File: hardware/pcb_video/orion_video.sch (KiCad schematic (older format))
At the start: 125 parts

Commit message: Оптимизирована логика видеовыхода
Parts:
- removed DD? (x3): LI1, Housings_SOIC:SOIC-14_3.9x8.7mm_Pitch1.27mm, symbol LI1
- added U?: 74AHC1G02, symbol 74AHC1G02
- added U?: 74AHC1G08, symbol 74AHC1G08
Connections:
- wire segments 937 -> 1030

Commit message: Завершена черновая схема видеомодуля.
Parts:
- removed DD? (x3): LI1, Housings_SOIC:SOIC-14_3.9x8.7mm_Pitch1.27mm, symbol LI1
- removed DD? (x6): LN1, Housings_SOIC:SOIC-14_3.9x8.7mm_Pitch1.27mm, symbol LN1-RESCUE-orion_video
- removed DD? (x2): KP11, Housings_SOIC:SOIC-16_3.9x9.9mm_Pitch1.27mm, symbol KP11
- removed DD? (x2): LA3, symbol LA3
- removed DD?: LL1, symbol LL1
- removed R?: 1k, Resistors_SMD:R_0805, symbol R_Small
- added C? (x16): 0.1u, Capacitors_SMD:C_0805, symbol C_Small
- added DD?: ATF22V10, symbol ATF22V10
- added J? (x5): 25M, Pin_Headers:Pin_Header_Straight_1x01_Pitch2.00mm, symbol TEST_1P
- added J? (x2): X0, Pin_Headers:Pin_Header_Straight_1x01_Pitch2.00mm, symbol TEST_1P
- added J? (x4): X4, Pin_Headers:Pin_Header_Straight_1x01_Pitch2.00mm, symbol TEST_1P
- added J?: MEM_W, symbol Conn_01x02
- added J?: MEM1, symbol Conn_02x12_Odd_Even
- added J?: MEM2, symbol Conn_02x12_Odd_Even
- added R?: 1k, Resistors_SMD:R_0805, symbol R_Small
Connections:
- net labels added: B0, CE0, CE1, FEN, HSP, MCP, MR, MW, OE, S16, S17, SL, SU, VC, WE, XR1, YR1, YR2, YR3, YR4
- net labels removed: CLKn, Gs, HS3, HS5, LBn, MA17, MA18, MA19n, MB0n, MB1n, MRn, MWn, OEn, SWE, U3, UBn, VA16n, VB0i, VB1i
- wire segments 1030 -> 997
- no-connect marks 0 -> 22
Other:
- moved on the sheet: C?, DD?, J?, U?

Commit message: Обновлена схема видеомодуля
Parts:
- removed C? (x6): 0.1u, Capacitors_SMD:C_0805, symbol C_Small
- removed DD? (x2): AP5, symbol AP5
- removed J?: X4, Pin_Headers:Pin_Header_Straight_1x01_Pitch2.00mm, symbol TEST_1P
- removed J?: MEM_W, symbol Conn_01x02
- removed J?: GDS, symbol Conn_02x08_Counter_Clockwise
- removed R? (x14): 2R, Resistors_SMD:R_0805, symbol R_Small
- removed R? (x8): R, Resistors_SMD:R_0805, symbol R_Small
- removed R?: 1k, Resistors_SMD:R_0805, symbol R_Small
- removed U?: 74AHC1G02, symbol 74AHC1G02
- removed U?: 74AHC1G08, symbol 74AHC1G08
- added JP1: 4:3, Socket_Strips:Socket_Strip_Straight_1x02_Pitch2.54mm, symbol Jumper_NC_Small
- added JP2: GDS, Socket_Strips:Socket_Strip_Straight_2x08_Pitch2.54mm, symbol Conn_02x08_Odd_Even
- added R10, R11, R12, R8, R9: 470, Resistors_SMD:R_0805, symbol R_Small
- added R14, R15, R3: 1k, Resistors_SMD:R_0805, symbol R_Small
- added R16, R17, R18: 510, Resistors_SMD:R_0805, symbol R_Small
- DD11, DD12, DD13, DD14, DD15, DD16: renamed from DD?; footprint (none) -> Housings_SOIC:SOIC-20W_7.5x12.8mm_Pitch1.27mm
- DD18: renamed from U?; footprint (none) -> Sockets:PLCC44
- DD19, DD20, DD21, DD22: renamed from DD?; footprint (none) -> Housings_SOIC:SOIC-16W_5.3x10.2mm_Pitch1.27mm
- DD23, DD28, DD7, DD8: renamed from DD?; footprint (none) -> Housings_DIP:DIP-24_W7.62mm_Socket_LongPads
- DD31, DD32: renamed from DD?; footprint Projects:SOJ-36 -> andreil:SOJ-36
- J10, J11, J12, J13, J14, J15, J16, J17, J18, J19, J20, J21, J22, J23, J24, J25, J26, J27, J28, J29, J30, J6, J7, J8, J9: renamed from J?; footprint Pin_Headers:Pin_Header_Straight_1x01_Pitch2.00mm -> Socket_Strips:Socket_Strip_Straight_1x01_Pitch2.54mm
- J4, J5: renamed from J?; footprint (none) -> Socket_Strips:Socket_Strip_Straight_2x12_Pitch2.00mm
- R13: renamed from R?; value 2R -> 1k
- R7: renamed from R?; value R -> 470
- U1, U2: renamed from U?; footprint Projects:SOJ-44 -> andreil:SOJ-44
- gave numbers to parts that had none: 57
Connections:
- net labels removed: 10MHz, 5MHz, B2, B3, B4, DSn, G1, G2, G3, G4, I, R1, R2, R3, R4, YR, YR3, YR4
- wire segments 997 -> 921
- no-connect marks 22 -> 14
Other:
- moved on the sheet: C1, C10, C11, C12, C13, C14, C15, C16, C17, C18, C19, C2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

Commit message: Предварительное размещение элементов
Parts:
- removed J10, J11, J18, J19, J28, J29, J30: X4, Socket_Strips:Socket_Strip_Straight_1x01_Pitch2.54mm, symbol TEST_1P
- removed J12, J13, J14, J15, J20, J21, J22, J23, J24, J25, J6, J7: 25M, Socket_Strips:Socket_Strip_Straight_1x01_Pitch2.54mm, symbol TEST_1P
- removed J16, J17, J26, J27, J8, J9: X0, Socket_Strips:Socket_Strip_Straight_1x01_Pitch2.54mm, symbol TEST_1P
- DD19, DD20, DD21, DD22: footprint Housings_SOIC:SOIC-16W_5.3x10.2mm_Pitch1.27mm -> Housings_SOIC:SOIC-16_3.9x9.9mm_Pitch1.27mm
- J2: footprint Projects:ORION_BE_ST -> Socket_Strips:Socket_Strip_Straight_2x32_Pitch2.54mm
- J3: footprint Projects:ORION_BE_EX -> Socket_Strips:Socket_Strip_Straight_2x18_Pitch2.54mm
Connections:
- net labels added: WEN
- net labels removed: XR1
- wire segments 921 -> 896

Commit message: Исправления по схеме видеомодуля:
1) Заменён системный разъём на DIN 41612;
2) ПЗУ знакогенератора заменена на 28C512;
3) Добавлена коммутация подачи питания на пин 9 разъёма VGA.
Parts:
- removed DD18: 28C256, Sockets:PLCC44, symbol 28C256
- added DD18: 28C512, Housings_DIP:DIP-28_W15.24mm_Socket_LongPads, symbol 28C512
- added J6: VGAP, Socket_Strips:Socket_Strip_Straight_1x03_Pitch2.54mm, symbol Conn_01x03
- J2: footprint Socket_Strips:Socket_Strip_Straight_2x32_Pitch2.54mm -> orion:DIN41612_B064M
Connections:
- wire segments 896 -> 899
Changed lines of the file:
@@
 LIBS:orion
 LIBS:74xgxx
+LIBS:memory
 LIBS:orion_video-cache
 EELAYER 25 0
@@
 F 0 "J2" H 8150 3950 50  0000 C CNN
 F 1 "SYS_PRO" H 8150 650 50  0000 C CNN
-F 2 "Socket_Strips:Socket_Strip_Straight_2x32_Pitch2.54mm" H 8100 2350 50  0001 C CNN
+F 2 "orion:DIN41612_B064M" H 8100 2350 50  0001 C CNN
 F 3 "" H 8100 2350 50  0001 C CNN
 	1    8100 2350
@@
 FL0
 $Comp
-L 28C256 DD18
-U 1 1 5AFFDE7E
-P 4800 9950
-F 0 "DD18" H 5000 10950 50  0000 C CNN
-F 1 "28C256" H 4950 9050 50  0000 C CNN
-F 2 "Sockets:PLCC44" H 4800 9950 50  0001 C CNN
-F 3 "" H 4800 9950 50  0001 C CNN
-	1    4800 9950
-	1    0    0    -1
-$EndComp
-$Comp
 L GND #PWR027
 U 1 1 5B0059A2
@@
 	4100 8450 4400 8450
 Wire Wire Line
-	4150 10650 4150 10900
-Wire Wire Line
 	4150 10750 4200 10750
 Wire Wire Line
-	4200 10850 4150 10850
+	4150 10850 4200 10850
 Connection ~ 4150 10850
-Wire Wire Line
-	4200 10650 4150 10650
-Connection ~ 4150 10750
 Wire Bus Line
 	5650 1050 5650 11150
@@
 	6900 3200 7050 3200
 Wire Wire Line
-	6100 3400 6000 3400
+	5575 3400 6100 3400
 Wire Wire Line
 	6000 3300 6100 3300
@@
 L VCC #PWR038
 U 1 1 5B080DD3
-P 5950 3100
-F 0 "#PWR038" H 5950 2950 50  0001 C CNN
-F 1 "VCC" V 5950 3275 50  0000 C CNN
-F 2 "" H 5950 3100 50  0001 C CNN
-F 3 "" H 5950 3100 50  0001 C CNN
-	1    5950 3100
-	0    -1   -1   0
+P 5725 3200
+F 0 "#PWR038" H 5725 3050 50  0001 C CNN
+F 1 "VCC" V 5675 3250 50  0000 C CNN
+F 2 "" H 5725 3200 50  0001 C CNN
+F 3 "" H 5725 3200 50  0001 C CNN
+	1    5725 3200
+	0    1    1    0
 $EndComp
 Wire Wire Line
@@
 	1    0    0    -1
 $EndComp
+Wire Wire Line
+	4150 10750 4150 10900
+$Comp
+L Conn_01x03 J6
+U 1 1 5AF6EB0D
+P 5375 3300
+F 0 "J6" H 5375 3500 50  0000 C CNN
+F 1 "VGAP" H 5375 3100 50  0000 C CNN
+F 2 "Socket_Strips:Socket_Strip_Straight_1x03_Pitch2.54mm" H 5375 3300 50  0001 C CNN
+F 3 "" H 5375 3300 50  0001 C CNN
+	1    5375 3300
+	-1   0    0    -1
+$EndComp
+Wire Wire Line
+	5950 3100 5950 3300
+Wire Wire Line
+	5950 3300 5575 3300
+Wire Wire Line
+	5575 3200 5725 3200
+$Comp
+L 28C512 DD18
+U 1 1 5AF7563F
+P 4800 9950
+F 0 "DD18" H 5000 10950 50  0000 C CNN
+F 1 "28C512" H 4950 8950 50  0000 C CNN
+F 2 "Housings_DIP:DIP-28_W15.24mm_Socket_LongPads" H 4800 9950 50  0001 C CNN
+F 3 "" H 4800 9950 50  0001 C CNN
+	1    4800 9950
+	1    0    0    -1
+$EndComp
+Entry Wire Line
+	4000 10650 4100 10550
+Text Label 4100 10550 0    60   ~ 0
+PGD
+Wire Wire Line
+	4100 10550 4200 10550
 $EndSCHEMATC

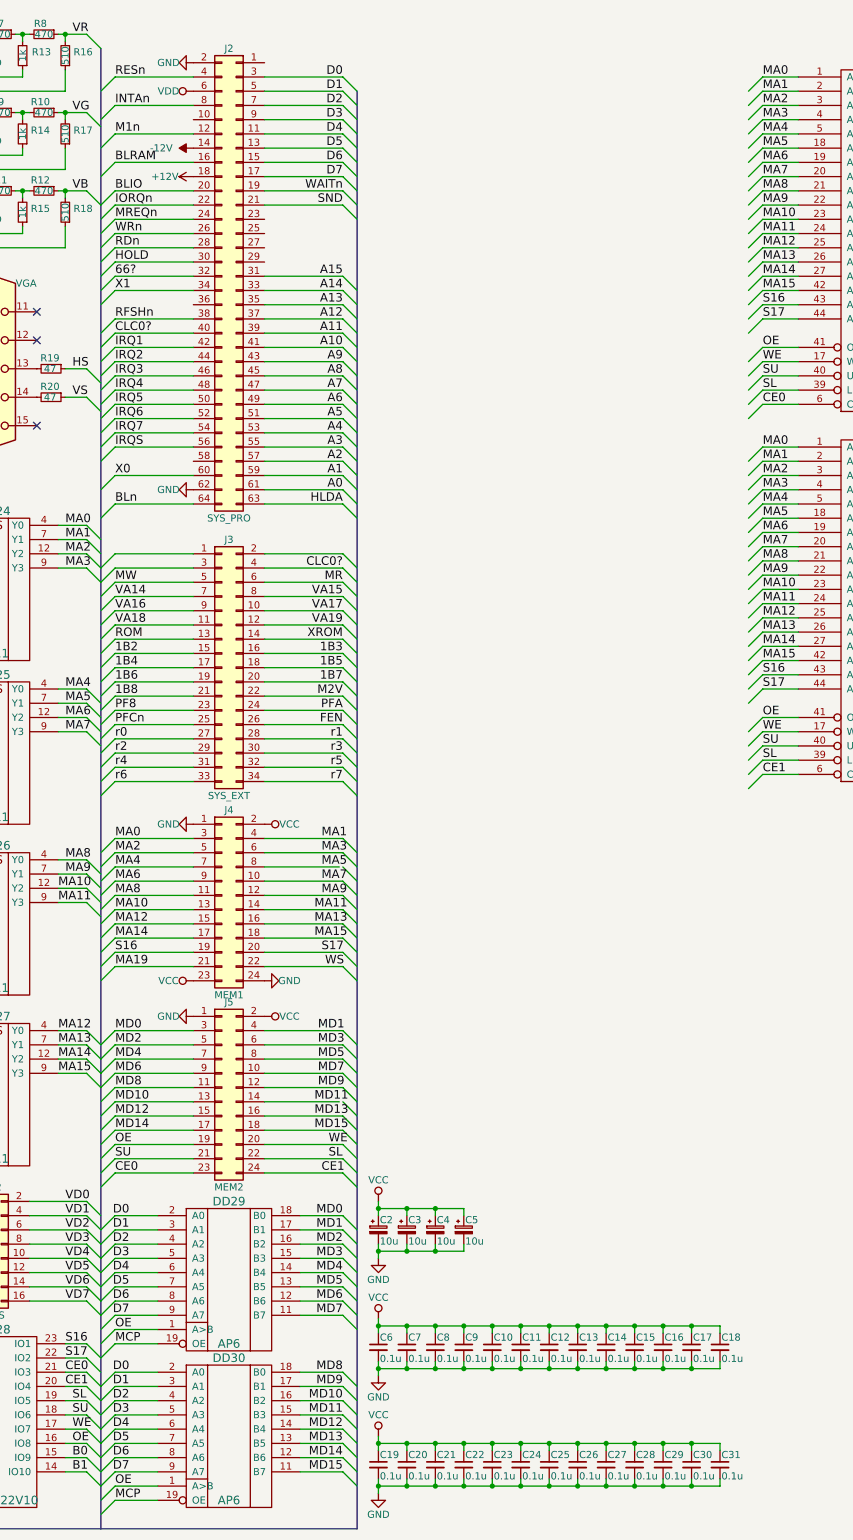
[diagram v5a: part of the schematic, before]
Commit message: Исправлен системный разъём - выполнен 3-х рядным DIN
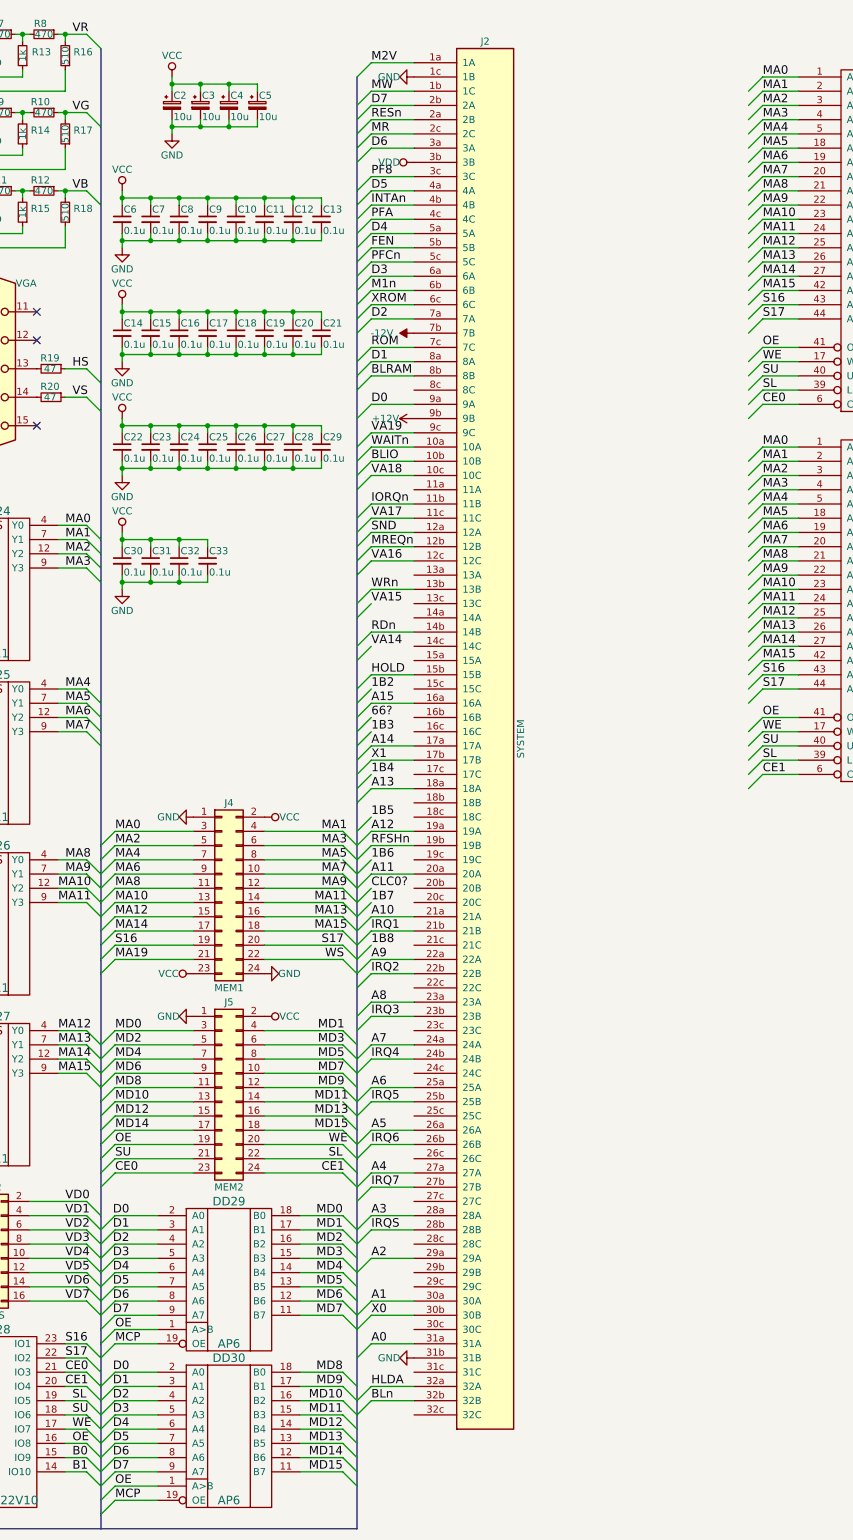
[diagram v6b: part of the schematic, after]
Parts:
- removed J2: SYS_PRO, orion:DIN41612_B064M, symbol Conn_02x32_Odd_Even
- removed J3: SYS_EXT, Socket_Strips:Socket_Strip_Straight_2x18_Pitch2.54mm, symbol Conn_02x17_Odd_Even
- added C32, C33: 0.1u, Capacitors_SMD:C_0805, symbol C_Small
- added J2: SYSTEM, Connectors_IEC_DIN:Socket_DIN41612-CaseC1-full-Male-96Pin-3rows, symbol C96ABC
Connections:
- net +12V: now also J2.9b (9B)
- net -12V: now also J2.7b (7B)
- net A0: now also J2.31a (31A)
- net A1: now also J2.30a (30A)
- net A10: now also J2.21a (21A)
- net A11: now also J2.20a (20A)
- net A12: now also J2.19a (19A)
- net A13: now also J2.18a (18A)
- net A14: now also J2.17a (17A)
- net A15: now also J2.16a (16A)
- net A2: now also J2.29a (29A)
- net A3: now also J2.28a (28A)
- net A4: now also J2.27a (27A)
- net A5: now also J2.26a (26A)
- net A6: now also J2.25a (25A)
- net A7: now also J2.24a (24A)
- net A8: now also J2.23a (23A)
- net A9: now also J2.22a (22A)
- net BLIO: now also J2.10b (10B)
- net BLRAM: now also J2.8b (8B)
- net BLn: now also J2.32b (32B)
- net D0: now also J2.9a (9A)
- net D1: now also J2.8a (8A)
- net D2: now also J2.7a (7A)
- net D3: now also J2.6a (6A)
- net D4: now also J2.5a (5A)
- net D5: now also J2.4a (4A)
- net D6: now also J2.3a (3A)
- net D7: now also J2.2b (2A)
- net FEN: now also J2.5b (5B)
- net GND: now also C32.2, C33.2, J2.1c (1B), J2.31b (31B)
- net HLDA: now also J2.32a (32A)
- net HOLD: now also J2.15b (15B)
- net INTAn: now also J2.4b (4B)
- net IORQn: now also J2.11b (11B)
- net IRQ1: now also J2.21b (21B)
- net IRQ2: now also J2.22b (22B)
- net IRQ3: now also J2.23b (23B)
- net IRQ4: now also J2.24b (24B)
- net IRQ5: now also J2.25b (25B)
- net IRQ6: now also J2.26b (26B)
- net IRQ7: now also J2.27b (27B)
- net IRQS: now also J2.28b (28B)
- net M1n: now also J2.6b (6B)
- net M2V: now also J2.1a (1A)
- net MR: now also J2.2c (2C)
- net MREQn: now also J2.12b (12B)
- net MW: now also J2.1b (1C)
- net PF8: now also J2.3c (3C)
- net PFA: now also J2.4c (4C)
- net PFCn: now also J2.5c (5C)
- net RDn: now also J2.14b (14B)
- net RESn: now also J2.2a (2B)
- net RFSHn: now also J2.19b (19B)
- net ROM: now also J2.7c (7C)
- net SND: now also J2.12a (12A)
- net VA16: now also J2.12c (12C)
- net VA17: now also J2.11c (11C)
- net VA18: now also J2.10c (10C)
- net VA19: now also J2.9c (9C)
- net VCC: now also C32.1, C33.1
- net VDD: now also J2.3b (3B)
- net WAITn: now also J2.10a (10A)
- net WRn: now also J2.13b (13B)
- net X0: now also J2.30b (30B)
- net X1: now also J2.17b (17B)
- net XROM: now also J2.6c (6C)
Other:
- moved on the sheet: C10, C11, C12, C13, C14, C15, C16, C17, C18, C19, C2, C20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
